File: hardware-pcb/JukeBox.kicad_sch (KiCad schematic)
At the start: 91 parts, among them J1 USB4105-GF-A, Q1 Q_NPN_ECB, SW1 SW_SPST, SW10 SW_SPST, SW11 SW_SPST, SW12 SW_SPST, SW2 SW_SPST, SW3 SW_SPST, SW4 SW_SPST, SW5 SW_SPST, SW6 SW_SPST, SW7 SW_SPST, SW8 SW_SPST, SW9 SW_SPST, U1 NCP1117-3.3_SOT223, U2 W25Q128JVS, U3 RP2040, U4 st7789v, Y1 ECS-120-20-33-AEL-TR

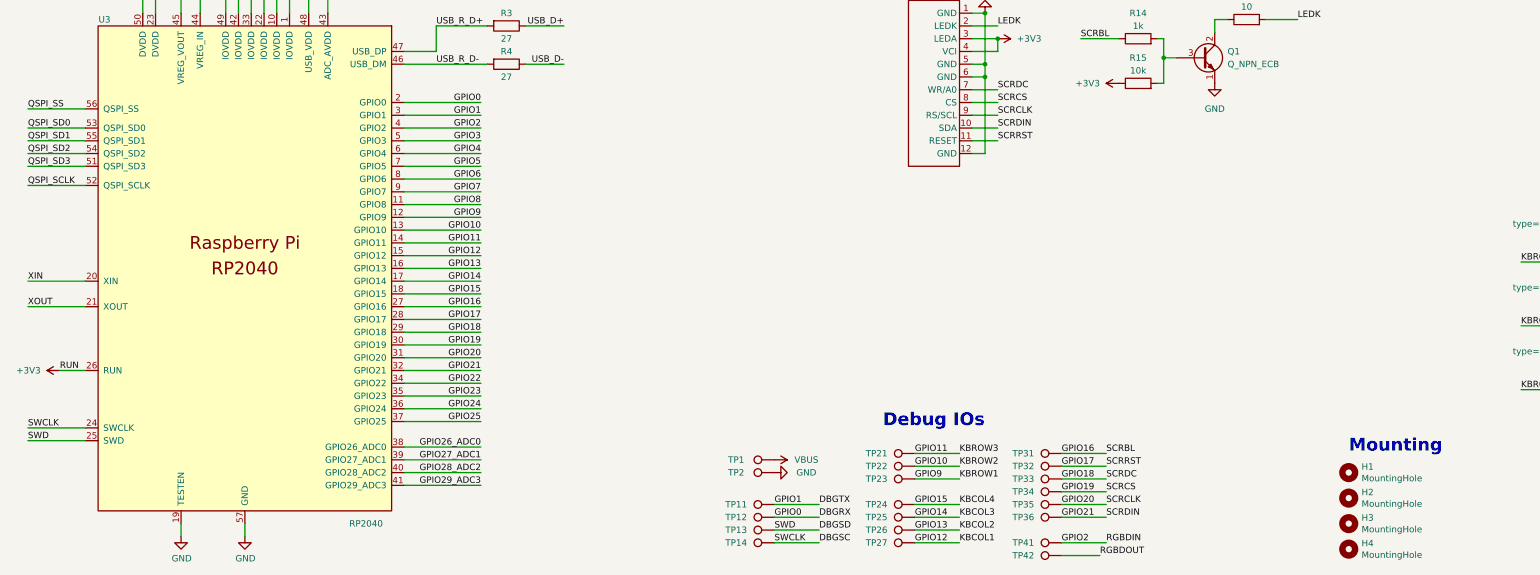
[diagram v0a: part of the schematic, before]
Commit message: rearrange parts, fix nets
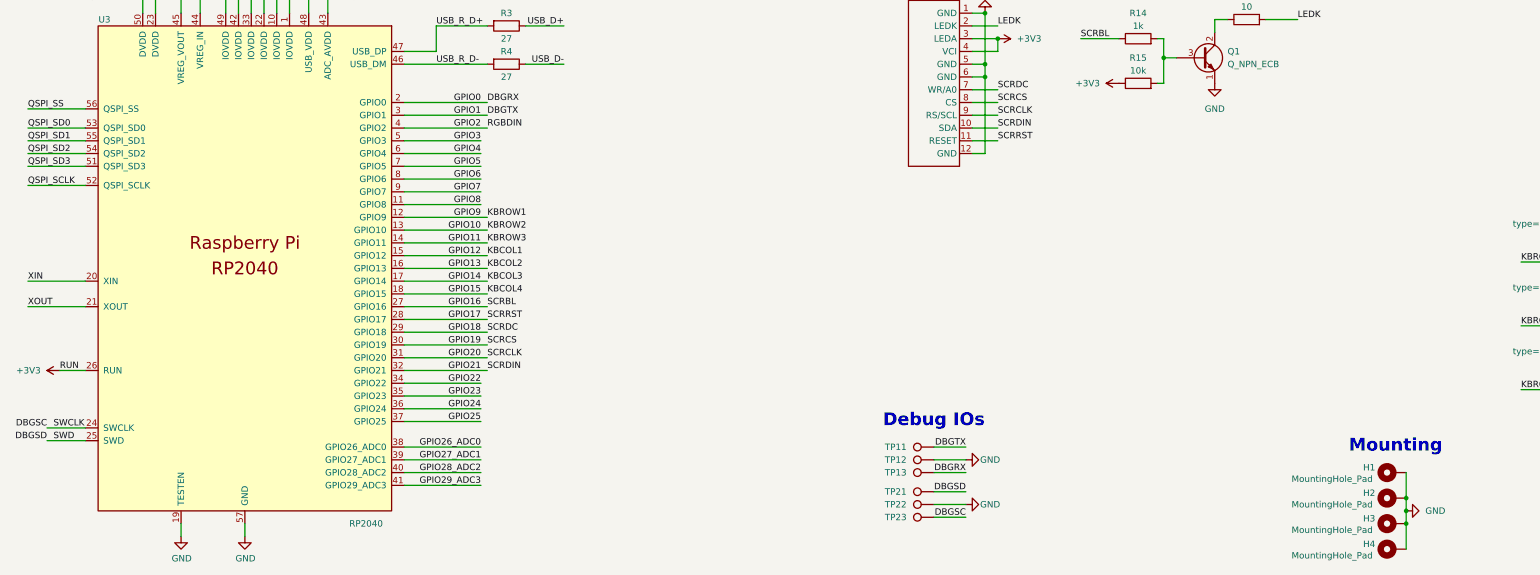
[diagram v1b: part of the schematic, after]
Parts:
- removed H1, H2, H3, H4: MountingHole, MountingHole:MountingHole_3.2mm_M3_Pad_Via, symbol Mechanical:MountingHole
- removed TP1, TP21, TP23, TP24, TP25, TP26, TP27, TP31, TP32, TP33, TP34, TP35, TP36, TP41, TP42: TestPoint, TestPoint:TestPoint_Pad_D1.0mm, symbol Connector:TestPoint
- added H1, H2, H3, H4: MountingHole_Pad, MountingHole:MountingHole_3.2mm_M3_Pad_Via, symbol Mechanical:MountingHole_Pad
- renumbered TP2 to TP12, TP12 to TP13, TP13 to TP21, TP14 to TP23
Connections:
- net GND: now also TP22.1, H1.1, H2.1, H3.1, H4.1
- net GPIO10: no longer TP22.1
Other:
- moved on the sheet: TP11, TP12, TP13, TP21, TP23

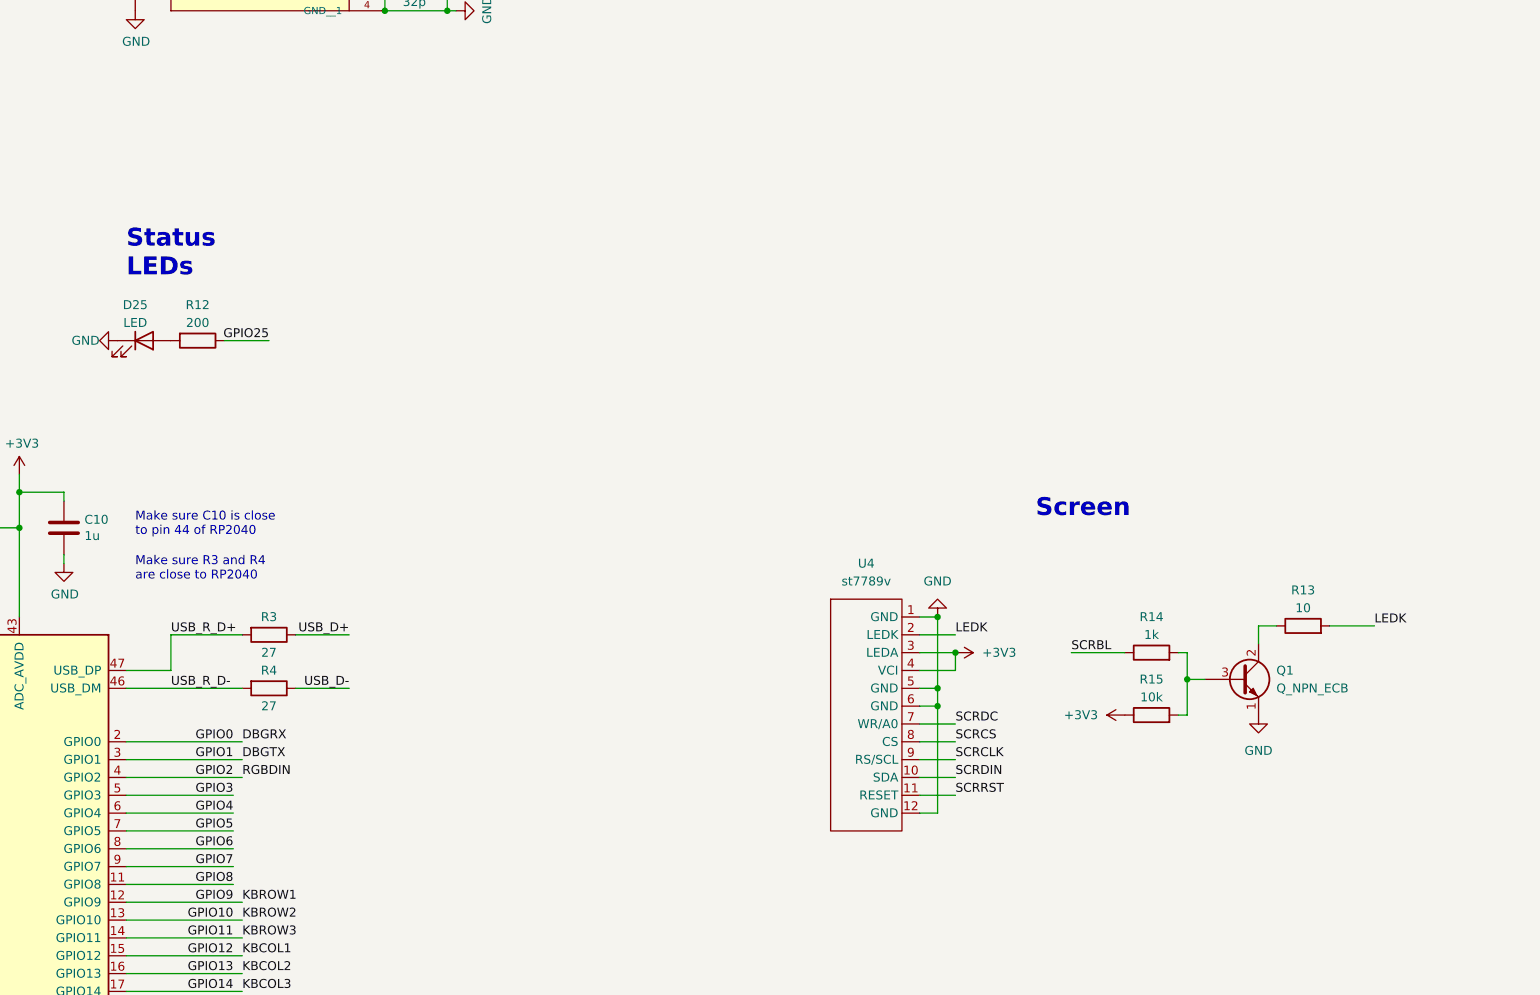
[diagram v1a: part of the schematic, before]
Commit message: add headphone jacks for i2c busses for expansion
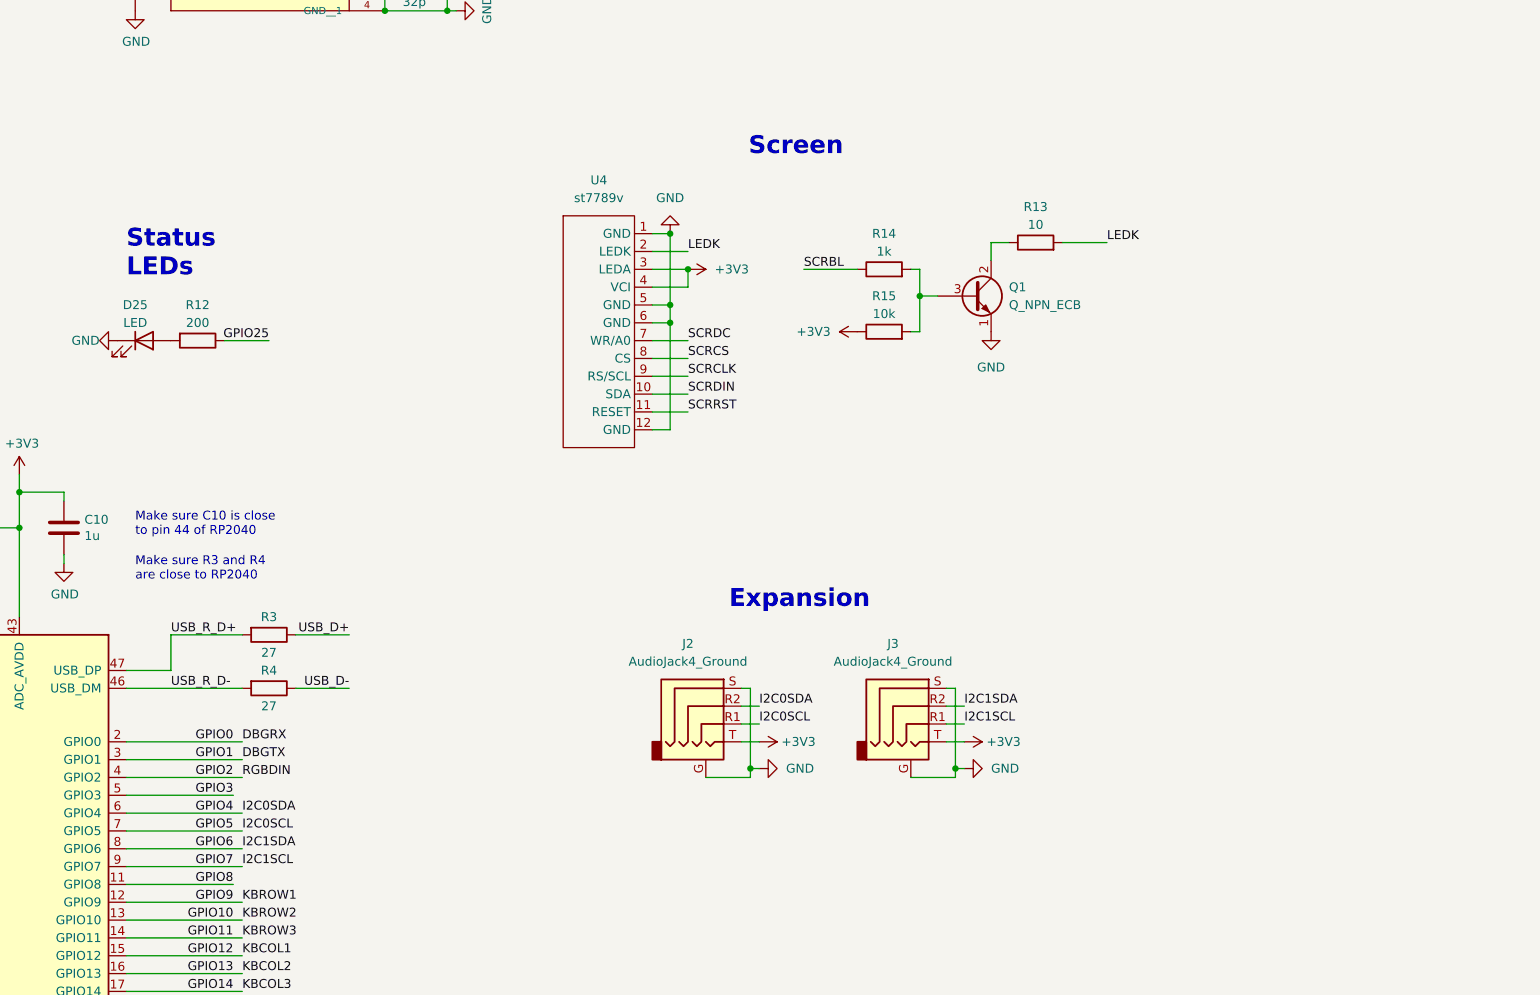
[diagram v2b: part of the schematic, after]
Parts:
- added J2, J3: AudioJack4_Ground, Connector_Audio:Jack_3.5mm_PJ320E_Horizontal, symbol Connector_Audio:AudioJack4_Ground
- TP11, TP12, TP13, TP21, TP22, TP23: footprint TestPoint:TestPoint_Pad_D1.0mm -> TestPoint:TestPoint_Pad_D1.5mm
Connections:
- net +3V3: now also J2.T, J3.T
- net GND: now also J2.G, J2.S, J3.G, J3.S
- net GPIO4: now also J2.R2
- net GPIO5: now also J2.R1
- net GPIO6: now also J3.R2
- net GPIO7: now also J3.R1
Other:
- note added: "Expansion"
- moved on the sheet: Q1, R13, R14, R15, U4

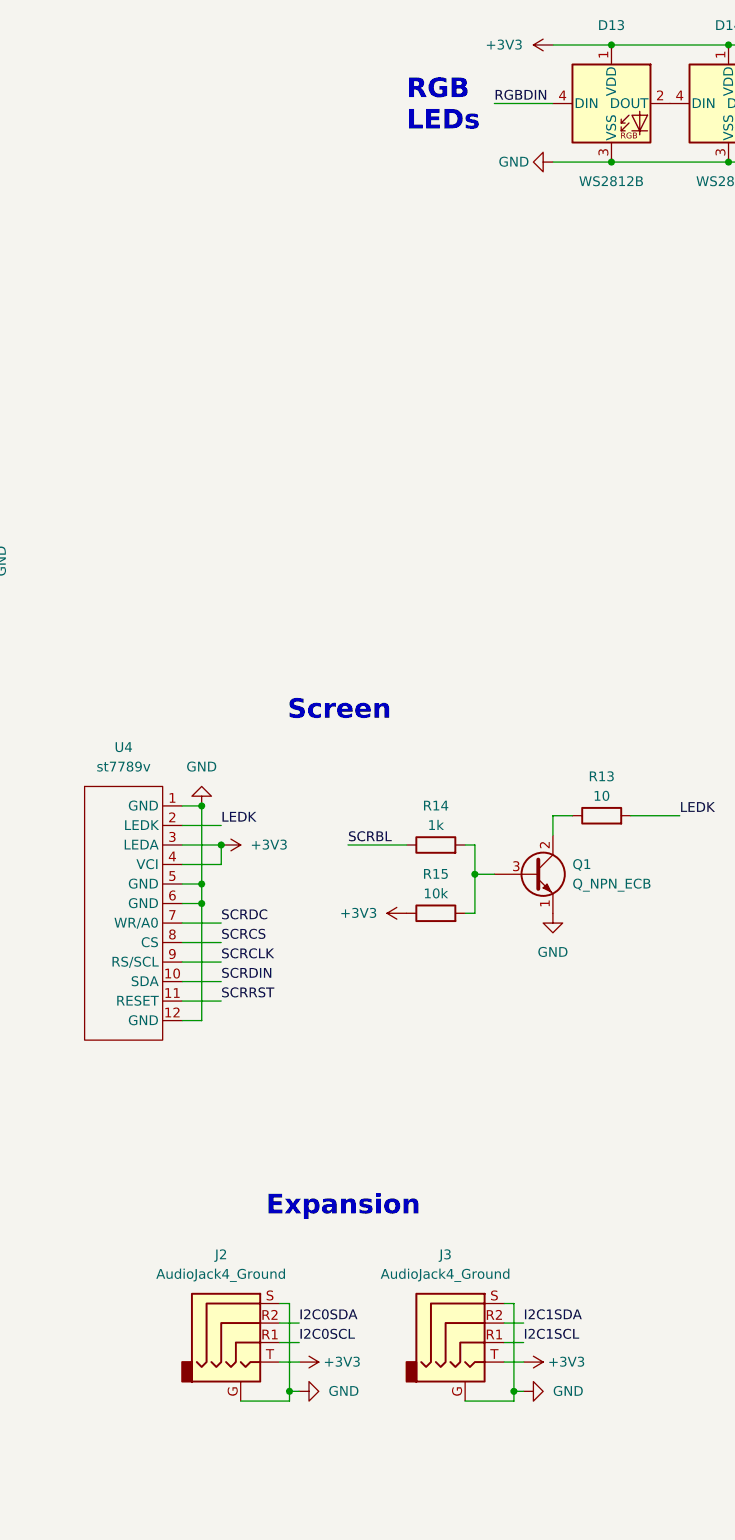
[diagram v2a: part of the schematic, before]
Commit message: fix screen footprint, prepare for fab
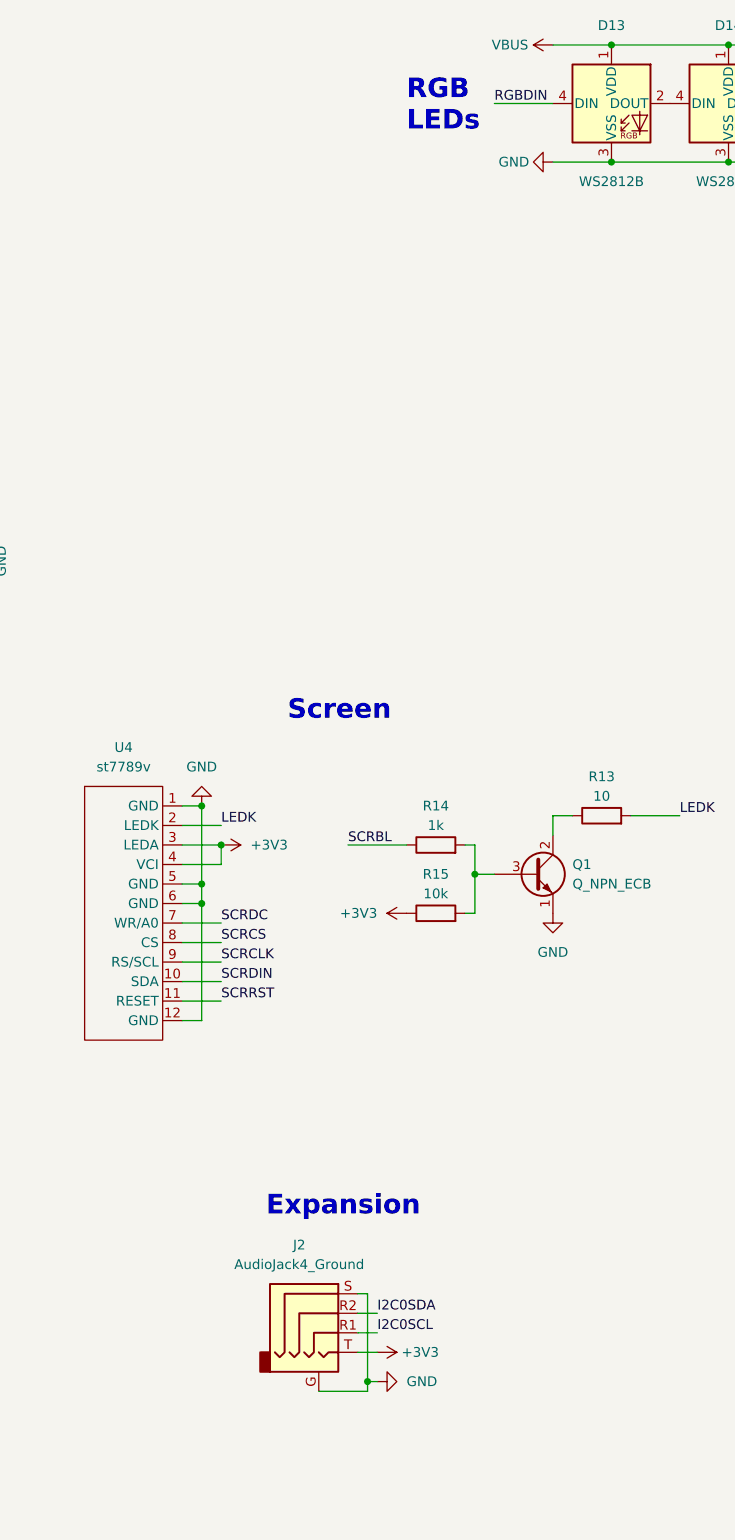
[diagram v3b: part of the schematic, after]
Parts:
- removed J3: AudioJack4_Ground, Connector_Audio:Jack_3.5mm_PJ320E_Horizontal, symbol Connector_Audio:AudioJack4_Ground
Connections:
- net +3V3: no longer D13.1 (VDD), D14.1 (VDD), D15.1 (VDD), D16.1 (VDD), D17.1 (VDD), D18.1 (VDD), D19.1 (VDD), D20.1 (VDD), D21.1 (VDD), D22.1 (VDD), D23.1 (VDD), D24.1 (VDD)
- net VBUS: now also D13.1 (VDD), D14.1 (VDD), D15.1 (VDD), D16.1 (VDD), D17.1 (VDD), D18.1 (VDD), D19.1 (VDD), D20.1 (VDD), D21.1 (VDD), D22.1 (VDD), D23.1 (VDD), D24.1 (VDD)
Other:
- moved on the sheet: J2

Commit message: minor updates for production
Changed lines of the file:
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@@
 			)
 		)
-		(property "Sim.Params" "type=\"D\" model=\"DIODE\" lib=\"\""
+		(property "Sim.Params" "1N4148W"
 			(at 0 0 0)
 			(effects
@@
 			)
 		)
-		(property "Sim.Params" "type=\"D\" model=\"DIODE\" lib=\"\""
+		(property "Sim.Params" "1N4148W"
 			(at 0 0 0)
 			(effects
@@
 			)
 		)
-		(property "Sim.Params" "type=\"D\" model=\"DIODE\" lib=\"\""
+		(property "Sim.Params" "1N4148W"
 			(at 0 0 0)
 			(effects
@@
 			)
 		)
-		(property "Sim.Params" "type=\"D\" model=\"DIODE\" lib=\"\""
+		(property "Sim.Params" "1N4148W"
 			(at 0 0 0)
 			(effects
@@
 			)
 		)
-		(property "Sim.Params" "type=\"D\" model=\"DIODE\" lib=\"\""
+		(property "Sim.Params" "1N4148W"
 			(at 0 0 0)
 			(effects
@@
 			)
 		)
-		(property "Sim.Params" "type=\"D\" model=\"DIODE\" lib=\"\""
+		(property "Sim.Params" "1N4148W"
 			(at 0 0 0)
 			(effects
@@
 			)
 		)
-		(property "Sim.Params" "type=\"D\" model=\"DIODE\" lib=\"\""
+		(property "Sim.Params" "1N4148W"
 			(at 0 0 0)
 			(effects
@@
 			)
 		)
-		(property "Sim.Params" "type=\"D\" model=\"DIODE\" lib=\"\""
+		(property "Sim.Params" "1N4148W"
 			(at 0 0 0)
 			(effects
@@
 			)
 		)
-		(property "Sim.Params" "type=\"D\" model=\"DIODE\" lib=\"\""
+		(property "Sim.Params" "1N4148W"
 			(at 0 0 0)
 			(effects
@@
 			)
 		)
-		(property "Sim.Params" "type=\"D\" model=\"DIODE\" lib=\"\""
+		(property "Sim.Params" "1N4148W"
 			(at 0 0 0)
 			(effects
@@
 			)
 		)
-		(property "Sim.Params" "type=\"D\" model=\"DIODE\" lib=\"\""
+		(property "Sim.Params" "1N4148W"
 			(at 0 0 0)
 			(effects
@@
 			)
 		)
-		(property "Sim.Params" "type=\"D\" model=\"DIODE\" lib=\"\""
+		(property "Sim.Params" "1N4148W"
 			(at 0 0 0)
 			(effects
